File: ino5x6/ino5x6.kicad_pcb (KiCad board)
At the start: 2 copper layers, 120 x 125 mm, 78 parts, among them J1 Conn_01x04_Male, J2 Conn_01x01_Male, J3 Conn_01x01_Male, J4 Conn_01x01_Male, J5 Conn_01x01_Male, SW1 SW_Push, SW10 SW_Push, SW11 SW_Push, SW12 SW_Push, SW13 SW_Push, SW14 SW_Push, SW15 SW_Push, SW16 SW_Push, SW17 SW_Push, SW18 SW_Push, SW19 SW_Push, SW2 SW_Push, SW20 SW_Push, SW21 SW_Push, SW22 SW_Push, SW23 SW_Push, SW24 SW_Push, SW25 SW_Push, SW26 SW_Push, SW27 SW_Push, SW28 SW_Push, SW29 SW_Push, SW3 SW_Push, SW30 SW_Push, SW4 SW_Push, SW5 SW_Push, SW6 SW_Push, SW7 SW_Push, SW8 SW_Push, SW9 SW_Push, U1 ProMicro

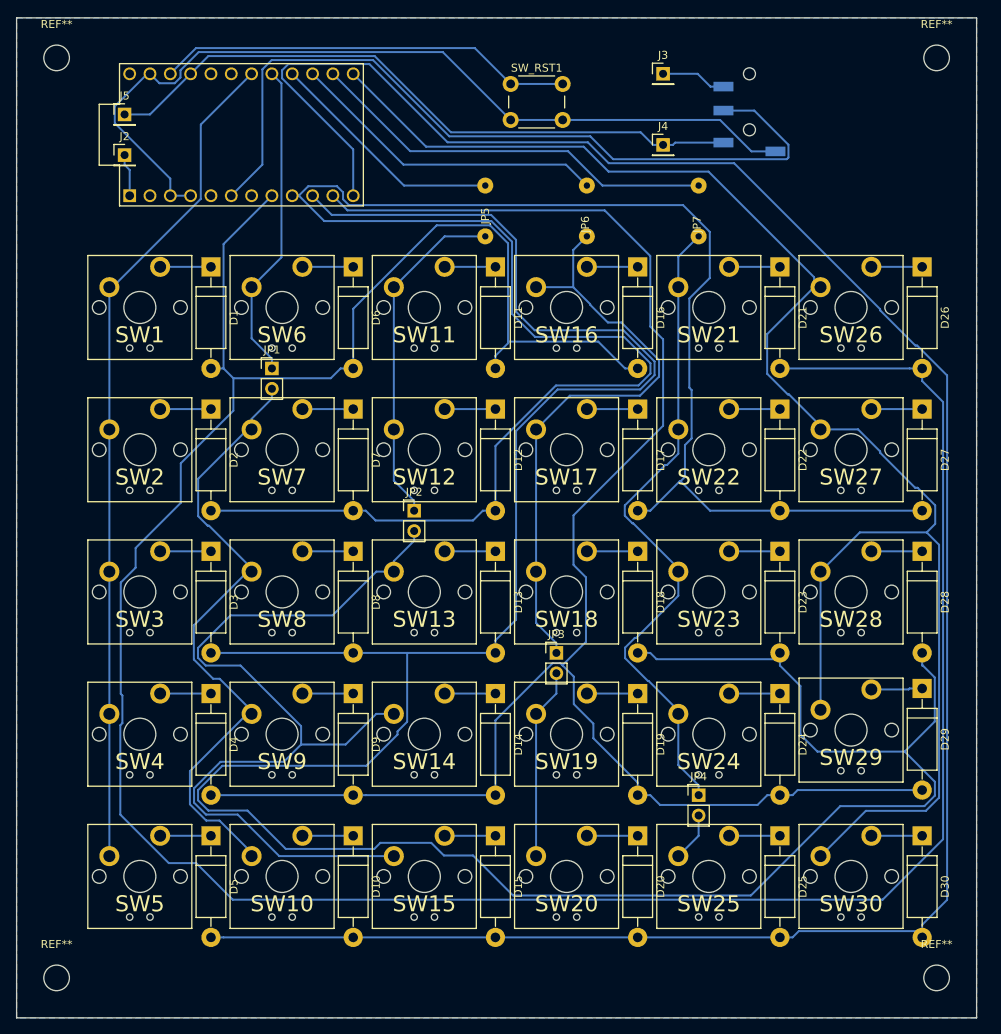
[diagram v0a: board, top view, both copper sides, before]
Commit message: 配置の厳密化
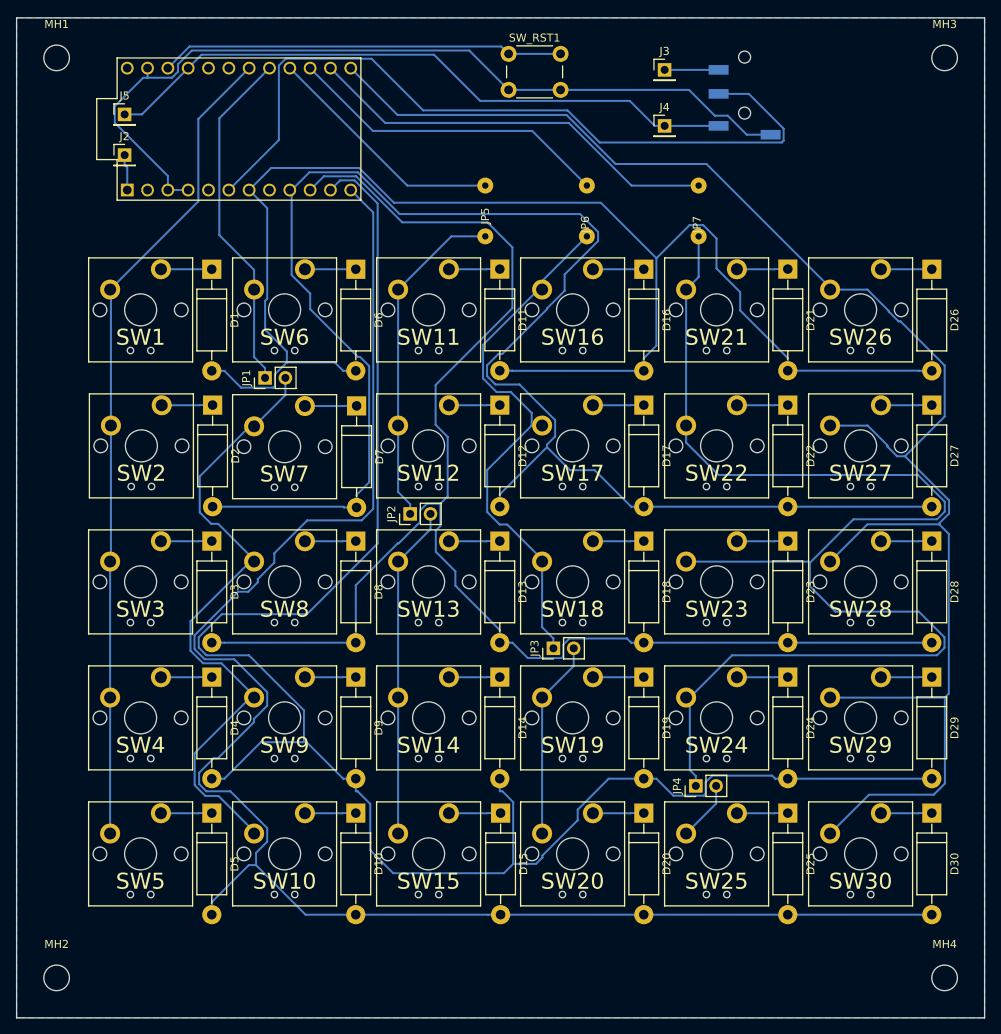
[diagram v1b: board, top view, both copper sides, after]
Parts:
- removed REF** (x4): MountingHole_3.2mm_M3, Mounting_Holes:MountingHole_3.2mm_M3
- added MH1: MountingHole, Mounting_Holes:MountingHole_3.2mm_M3, F.Cu at (55.0, 45.0)
- added MH2: MountingHole, Mounting_Holes:MountingHole_3.2mm_M3, F.Cu at (55.0, 160.0)
- added MH3: MountingHole, Mounting_Holes:MountingHole_3.2mm_M3, F.Cu at (166.0, 45.0)
- added MH4: MountingHole, Mounting_Holes:MountingHole_3.2mm_M3, F.Cu at (166.0, 160.0)
- moved SW_RST1 3.77 mm to (111.5, 44.5)
- moved D30 3.09 mm to (164.4, 139.4)
- moved SW30 3.06 mm to (155.5, 144.5)
- moved D25 3.01 mm to (146.4, 139.4)
- moved SW25 2.98 mm to (137.5, 144.5)
- moved D20 2.94 mm to (128.4, 139.4)
- moved SW20 2.92 mm to (119.5, 144.5)
- moved D15 2.91 mm to (110.5, 139.4)
- moved SW15 2.87 mm to (101.5, 144.5)
- moved D10 2.86 mm to (92.4, 139.4)
- moved D5 2.84 mm to (74.4, 139.4)
- moved SW10 2.84 mm to (83.5, 144.5)
- moved SW5 2.82 mm to (65.5, 144.5)
- moved J4 2.39 mm to (131.0, 53.5)
- moved D24 2.28 mm to (146.4, 122.4)
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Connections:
- U1 pad 7: Net-(U1-Pad7) -> /row0
- U1 pad 8: /row0 -> Net-(U1-Pad8)
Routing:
- net /row0: track 357.5 -> 182.8 mm
- net /row2: track 350.4 -> 185.3 mm
- net Net-(JP4-Pad1): track 83.3 -> 168.0 mm
- net Net-(JP2-Pad2): track 112.9 -> 41.6 mm
- net /row4: track 279.8 -> 211.2 mm
- net /row1: track 254.1 -> 204.8 mm
- net /row3: track 214.5 -> 222.3 mm
- net Net-(JP3-Pad1): track 75.4 -> 68.3 mm
- net /col5: track 199.6 -> 205.5 mm
- net /col1: track 39.9 -> 43.7 mm
- net /sda: track 100.4 -> 97.5 mm
- net /col0: track 105.4 -> 103.0 mm
- net GND: track 108.6 -> 106.7 mm
- net Net-(SW_RST1-Pad1): track 52.2 -> 50.6 mm
- net VCC: track 82.6 -> 81.0 mm
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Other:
- board size 120 x 125 mm -> 121 x 125 mm

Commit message: クリアランスと太さを0.3に
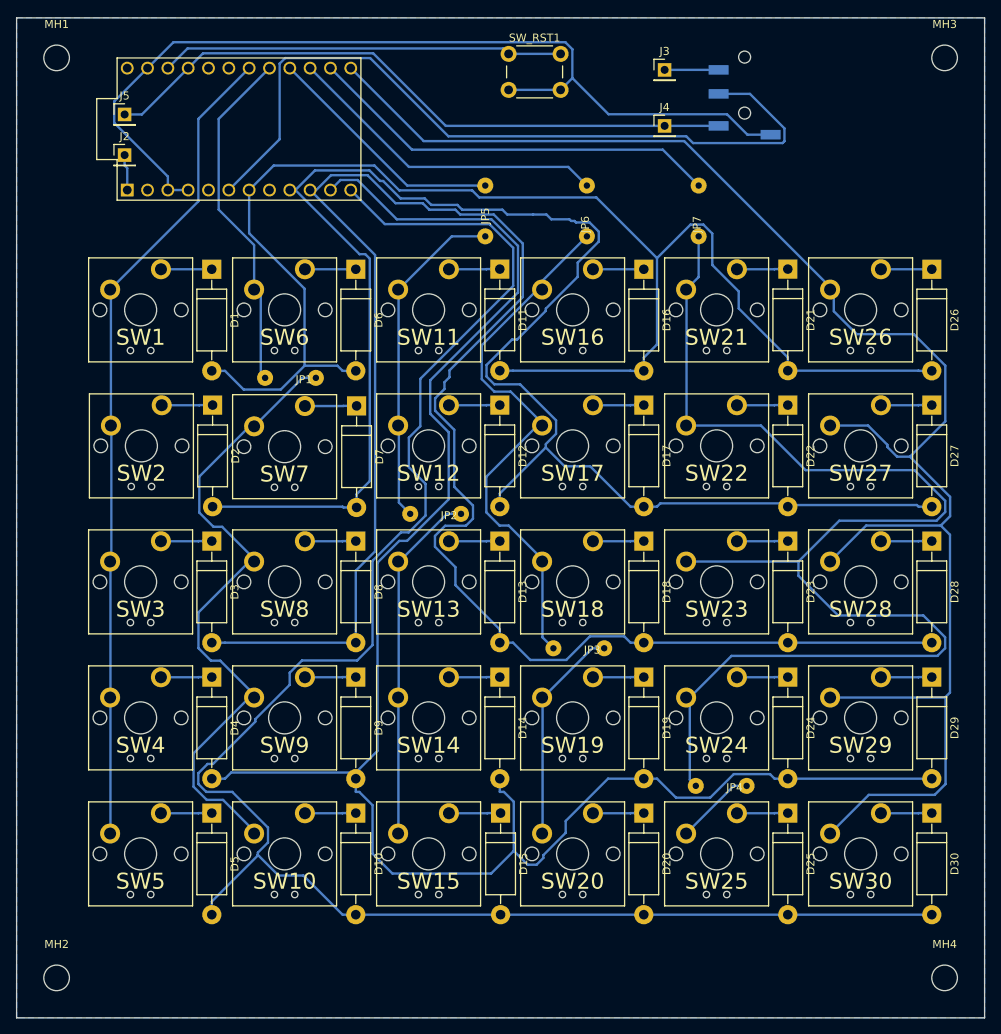
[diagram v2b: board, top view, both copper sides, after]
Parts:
- JP1, JP2, JP3, JP4: footprint Pin_Headers:Pin_Header_Straight_1x02_Pitch2.54mm -> Wire_Connections_Bridges:WireConnection_0.80mmDrill
- turned JP1 to 0 degrees
- turned JP2 to 0 degrees
- turned JP3 to 0 degrees
- turned JP4 to 0 degrees
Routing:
- net /row2: track 185.3 -> 229.3 mm
- net /row4: track 211.2 -> 225.4 mm
- net GND: track 106.7 -> 117.0 mm
- net Net-(JP2-Pad2): track 41.6 -> 44.4 mm
- net Net-(JP3-Pad2): track 24.8 -> 27.3 mm
- net Net-(JP4-Pad2): track 7.51 -> 10.0 mm
- net /row3: track 222.3 -> 224.5 mm
- net /col5: track 205.5 -> 207.5 mm
- net Net-(JP1-Pad2): track 80.3 -> 81.9 mm
- net /row1: track 204.8 -> 206.4 mm
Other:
- net class Default: clearance 0.25 -> 0.3; trace_width 0.25 -> 0.3
- rule trace_clearance: 0.25 -> 0.3
